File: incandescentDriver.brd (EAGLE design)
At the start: 100.3 x 47.2 mm, 36 parts, among them IC2 7805, IC5 74LS595N, J1 HEADER, J10 HEADER, J11 POWER_JACKPTH_LOCK, J2 HEADER, J3 HEADER, J4 HEADER, J5 HEADER, J6 HEADER, J7 HEADER, J8 HEADER, J9 HEADER

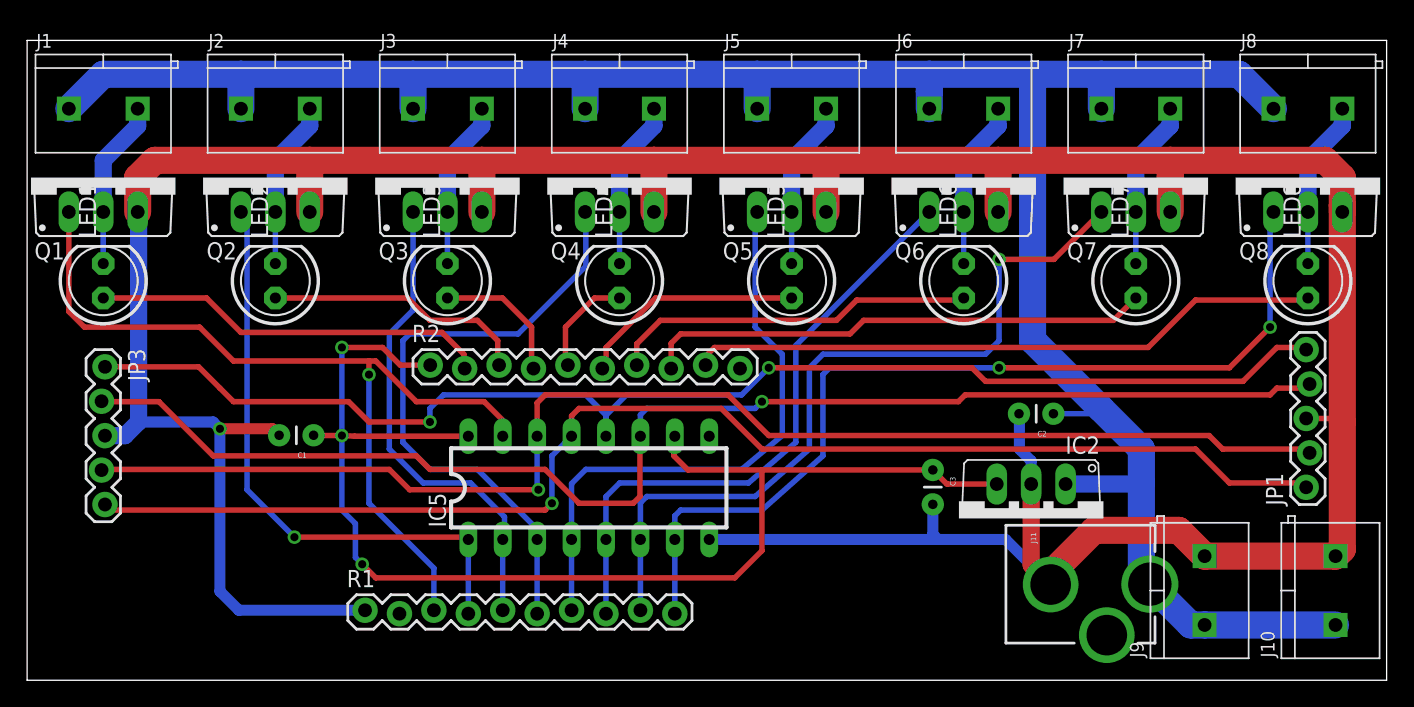
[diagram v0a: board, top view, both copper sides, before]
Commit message: updated incandescent driver to 1.0
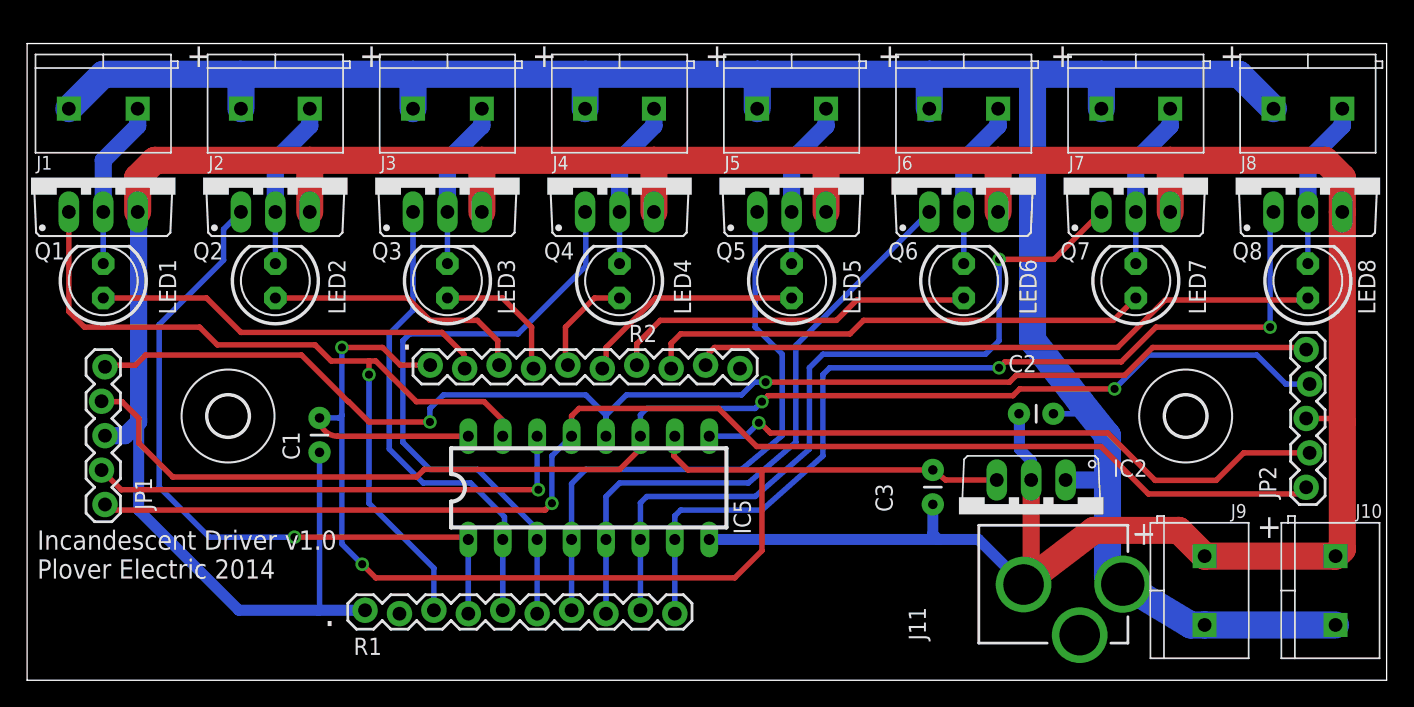
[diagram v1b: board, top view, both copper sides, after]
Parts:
- removed JP3: (no value), SparkFun-Connectors:1X05_LOCK
- added JP2: OUTPUT, SparkFun-Connectors:1X05_LOCK
- added U$1, U$2: (no value), holes:3,0
- J1: value HEADER -> LOAD 1
- J10, J9: value HEADER -> POWER
- J11: value POWER_JACKPTH_LOCK -> POWER INPUT
- J2: value HEADER -> LOAD 2
- J3: value HEADER -> LOAD 3
- J4: value HEADER -> LOAD 4
- J5: value HEADER -> LOAD 5
- J6: value HEADER -> LOAD 6
- J7: value HEADER -> LOAD 7
- J8: value HEADER -> LOAD 8
- JP1: value (none) -> INPUT
- R1: value 10K -> 10K-Array
- R2: value 1K -> 1K-Array
- moved JP1 89.3 mm to (5.62, 23.1), turned to 270 degrees
- moved J11 2.00 mm to (67.0, 7.09)
- moved C1 1.35 mm to (21.6, 19.4), turned to 270 degrees
- moved IC2 0.30 mm to (74.1, 12.2)
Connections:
- net DIN: now also JP1.4; no longer JP1.2, JP3.4
- net DOUT: now also JP2.2
- net G: now also JP1.5, JP2.1; no longer JP1.1, JP3.5
- net GND: now also JP2.3; no longer JP3.3
- net RCK: now also JP1.1, JP2.5; no longer JP1.5, JP3.1
- net SCK: now also JP1.2, JP2.4; no longer JP1.4, JP3.2
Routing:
- net DIN: track 98.4 -> 36.9 mm
- net DOUT: track 0.00 -> 47.3 mm, vias 0 -> 1
- net G2: track 44.3 -> 52.9 mm
- net GND: track 266.1 -> 268.6 mm, vias 1 -> 0
- net SCK: track 100.4 -> 98.7 mm, vias 1 -> 2
- net VCC: track 98.0 -> 99.7 mm, vias 3 -> 2
- net VCC24V: track 171.7 -> 170.8 mm
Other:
- board size 100.3 x 47.2 mm -> 100.3 x 47 mm
- board text added: "+"
- board text added: "."
- board text added: "Incandescent Driver v1.0 Plover Electric 2014"
